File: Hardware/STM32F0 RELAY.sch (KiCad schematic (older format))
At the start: 22 parts, among them Q2 Q_NMOS_GSD, U10 STM32F030RCT6, Y3 32.768kHz, Y4 8MHz

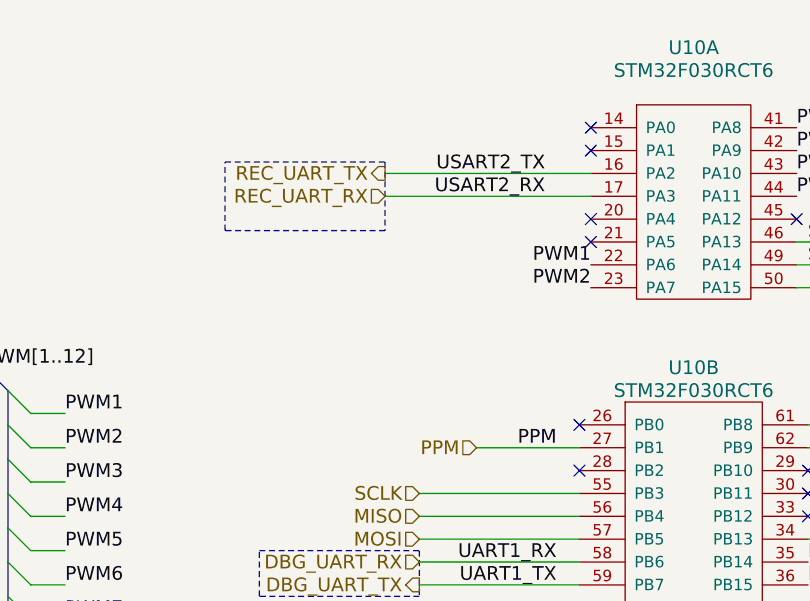
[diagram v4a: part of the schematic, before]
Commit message: Added RSSI, datasheets, INDU-004
Added RSSI input to PPM connector. Added datasheets for most of the components. The filter inductors for the FTDI were labeled as INDU-002, which is a 15uH smps inductor.
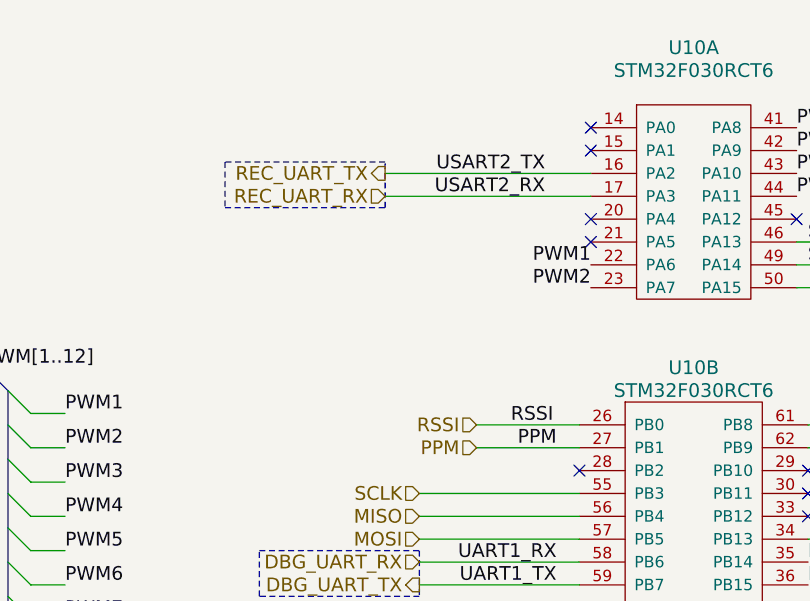
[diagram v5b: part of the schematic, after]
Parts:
- C46, C47, C48, C49, C50, C51, C52, C53, C54: footprint Resistors_SMD:R_0603_HandSoldering -> Capacitors_SMD:C_0603_HandSoldering
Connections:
- net RSSI: now reaches U10.26 (PB0)
- no-connect marks 18 -> 17
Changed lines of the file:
@@
 F 0 "C51" H 7225 5150 50  0000 L CNN
 F 1 "100nF" H 7225 4950 50  0000 L CNN
-F 2 "Resistors_SMD:R_0603_HandSoldering" H 7238 4900 50  0001 C CNN
-F 3 "" H 7200 5050 50  0001 C CNN
+F 2 "Capacitors_SMD:C_0603_HandSoldering" H 7238 4900 50  0001 C CNN
+F 3 "https://search.murata.co.jp/Ceramy/image/img/A01X/G101/ENG/GRM188R71E104KA01-01.pdf" H 7200 5050 50  0001 C CNN
 F 4 "CAPP-005" H 7200 5050 60  0001 C CNN "part_num"
 	1    7200 5050
@@
 F 0 "C52" H 7475 5150 50  0000 L CNN
 F 1 "4.7uF" H 7475 4950 50  0000 L CNN
-F 2 "Resistors_SMD:R_0603_HandSoldering" H 7488 4900 50  0001 C CNN
-F 3 "" H 7450 5050 50  0001 C CNN
+F 2 "Capacitors_SMD:C_0603_HandSoldering" H 7488 4900 50  0001 C CNN
+F 3 "http://www.samsungsem.com/kr/support/product-search/mlcc/CL10A475MP5LNNC.jsp" H 7450 5050 50  0001 C CNN
 F 4 "CAPP-006" H 7450 5050 60  0001 C CNN "part_num"
 	1    7450 5050
@@
 F 0 "C53" H 7725 5150 50  0000 L CNN
 F 1 "10nF" H 7725 4950 50  0000 L CNN
-F 2 "Resistors_SMD:R_0603_HandSoldering" H 7738 4900 50  0001 C CNN
-F 3 "" H 7700 5050 50  0001 C CNN
+F 2 "Capacitors_SMD:C_0603_HandSoldering" H 7738 4900 50  0001 C CNN
+F 3 "https://search.murata.co.jp/Ceramy/image/img/A01X/G101/ENG/GRM188R71H103KA01-01.pdf" H 7700 5050 50  0001 C CNN
 F 4 "CAPP-010" H 7700 5050 60  0001 C CNN "part_num"
 	1    7700 5050
@@
 F 0 "C50" H 6975 5150 50  0000 L CNN
 F 1 "100nF" H 6975 4950 50  0000 L CNN
-F 2 "Resistors_SMD:R_0603_HandSoldering" H 6988 4900 50  0001 C CNN
-F 3 "" H 6950 5050 50  0001 C CNN
+F 2 "Capacitors_SMD:C_0603_HandSoldering" H 6988 4900 50  0001 C CNN
+F 3 "https://search.murata.co.jp/Ceramy/image/img/A01X/G101/ENG/GRM188R71E104KA01-01.pdf" H 6950 5050 50  0001 C CNN
 F 4 "CAPP-005" H 6950 5050 60  0001 C CNN "part_num"
 	1    6950 5050
@@
 F 0 "C54" H 7975 5150 50  0000 L CNN
 F 1 "1uF" H 7975 4950 50  0000 L CNN
-F 2 "Resistors_SMD:R_0603_HandSoldering" H 7988 4900 50  0001 C CNN
-F 3 "" H 7950 5050 50  0001 C CNN
+F 2 "Capacitors_SMD:C_0603_HandSoldering" H 7988 4900 50  0001 C CNN
+F 3 "https://search.murata.co.jp/Ceramy/image/img/A01X/G101/ENG/GRM188R61E105KA12-01.pdf" H 7950 5050 50  0001 C CNN
 F 4 "CAPP-004" H 7950 5050 60  0001 C CNN "part_num"
 	1    7950 5050
@@
 F 1 "32.768kHz" H 7000 2150 50  0000 C CNN
 F 2 "Crystals:Crystal_SMD_MicroCrystal_CC7V-T1A-2pin_3.2x1.5mm_HandSoldering" H 7000 2300 50  0001 C CNN
-F 3 "" H 7000 2300 50  0001 C CNN
+F 3 "http://www.ecsxtal.com/store/pdf/ecx-31b.pdf" H 7000 2300 50  0001 C CNN
 F 4 "XTAL-001" H 7000 2300 60  0001 C CNN "part_num"
 	1    7000 2300
@@
 F 1 "8MHz" H 7000 2700 50  0000 C CNN
 F 2 "Crystals:Crystal_SMD_5032-2pin_5.0x3.2mm_HandSoldering" H 7000 2850 50  0001 C CNN
-F 3 "" H 7000 2850 50  0001 C CNN
+F 3 "https://abracon.com/Resonators/abm3.pdf" H 7000 2850 50  0001 C CNN
 F 4 "XTAL-002" H 7000 2850 60  0001 C CNN "part_num"
 	1    7000 2850
@@
 F 0 "C48" H 6575 2800 50  0000 L CNN
 F 1 "7pF" H 6575 2600 50  0000 L CNN
-F 2 "Resistors_SMD:R_0603_HandSoldering" H 6588 2550 50  0001 C CNN
-F 3 "" H 6550 2700 50  0001 C CNN
+F 2 "Capacitors_SMD:C_0603_HandSoldering" H 6588 2550 50  0001 C CNN
+F 3 "https://katalog.we-online.de/pbs/datasheet/885012006031.pdf" H 6550 2700 50  0001 C CNN
 F 4 "CAPP-009" H 6550 2700 60  0001 C CNN "part_num"
 	1    6550 2700
@@
 F 0 "C49" H 6575 3100 50  0000 L CNN
 F 1 "7pF" H 6575 2900 50  0000 L CNN
-F 2 "Resistors_SMD:R_0603_HandSoldering" H 6588 2850 50  0001 C CNN
-F 3 "" H 6550 3000 50  0001 C CNN
+F 2 "Capacitors_SMD:C_0603_HandSoldering" H 6588 2850 50  0001 C CNN
+F 3 "https://katalog.we-online.de/pbs/datasheet/885012006031.pdf" H 6550 3000 50  0001 C CNN
 F 4 "CAPP-009" H 6550 3000 60  0001 C CNN "part_num"
 	1    6550 3000
@@
 F 0 "C47" H 6575 2550 50  0000 L CNN
 F 1 "14pF" H 6575 2350 50  0000 L CNN
-F 2 "Resistors_SMD:R_0603_HandSoldering" H 6588 2300 50  0001 C CNN
-F 3 "" H 6550 2450 50  0001 C CNN
+F 2 "Capacitors_SMD:C_0603_HandSoldering" H 6588 2300 50  0001 C CNN
+F 3 "https://katalog.we-online.de/pbs/datasheet/885012006033.pdf" H 6550 2450 50  0001 C CNN
 F 4 "CAPP-008" H 6550 2450 60  0001 C CNN "part_num"
 	1    6550 2450
@@
 F 0 "C46" H 6575 2250 50  0000 L CNN
 F 1 "14pF" H 6575 2050 50  0000 L CNN
-F 2 "Resistors_SMD:R_0603_HandSoldering" H 6588 2000 50  0001 C CNN
-F 3 "" H 6550 2150 50  0001 C CNN
+F 2 "Capacitors_SMD:C_0603_HandSoldering" H 6588 2000 50  0001 C CNN
+F 3 "https://katalog.we-online.de/pbs/datasheet/885012006033.pdf" H 6550 2150 50  0001 C CNN
 F 4 "CAPP-008" H 6550 2150 60  0001 C CNN "part_num"
 	1    6550 2150
@@
 Wire Notes Line
 	2500 4400 3200 4400
-Wire Notes Line
-	3050 2700 3050 3000
-Wire Notes Line
-	3050 3000 2350 3000
-Wire Notes Line
-	2350 3000 2350 2700
-Wire Notes Line
-	2350 2700 3050 2700
 $Comp
 L Device:LED D8
@@
 F 1 "LED" H 5800 5650 50  0000 C CNN
 F 2 "LEDs:LED_0603" H 5800 5750 50  0001 C CNN
-F 3 "" H 5800 5750 50  0001 C CNN
+F 3 "http://optoelectronics.liteon.com/upload/download/DS22-2000-228/LTST-C191KGKT.PDF" H 5800 5750 50  0001 C CNN
 F 4 "DIOD-002" H 5800 5750 60  0001 C CNN "part_num"
 	1    5800 5750
@@
 F 1 "LED" H 5450 5650 50  0000 C CNN
 F 2 "LEDs:LED_0603" H 5450 5750 50  0001 C CNN
-F 3 "" H 5450 5750 50  0001 C CNN
+F 3 "http://optoelectronics.liteon.com/upload/download/DS22-2000-228/LTST-C191KGKT.PDF" H 5450 5750 50  0001 C CNN
 F 4 "DIOD-002" H 5450 5750 60  0001 C CNN "part_num"
 	1    5450 5750
@@
 F 1 "LED" H 6150 5650 50  0000 C CNN
 F 2 "LEDs:LED_0603" H 6150 5750 50  0001 C CNN
-F 3 "" H 6150 5750 50  0001 C CNN
+F 3 "http://optoelectronics.liteon.com/upload/download/DS22-2000-228/LTST-C191KGKT.PDF" H 6150 5750 50  0001 C CNN
 F 4 "DIOD-002" H 6150 5750 60  0001 C CNN "part_num"
 	1    6150 5750
@@
 F 1 "Buzzer" H 6750 3900 50  0000 L CNN
 F 2 "WARG:AI-1027-TWT-3V-R" V 6575 4050 50  0001 C CNN
-F 3 "" V 6575 4050 50  0001 C CNN
+F 3 "http://www.puiaudio.com/pdf/AI-1027-TWT-5V-R.pdf" V 6575 4050 50  0001 C CNN
 F 4 "BUZZ-001" H 6600 3950 60  0001 C CNN "part_num"
 	1    6600 3950
@@
 Connection ~ 8900 4350
 NoConn ~ 3900 4050
-NoConn ~ 3900 3850
 NoConn ~ 4900 4050
 NoConn ~ 4900 4150
@@
 Wire Wire Line
 	5800 4500 5800 4600
+Text HLabel 3450 3850 0    60   Input ~ 0
+RSSI
+Wire Wire Line
+	3450 3850 3900 3850
+Text Label 3600 3850 0    60   ~ 0
+RSSI
+Wire Notes Line
+	3050 2700 2350 2700
+Wire Notes Line
+	2350 2700 2350 2900
+Wire Notes Line
+	2350 2900 3050 2900
+Wire Notes Line
+	3050 2900 3050 2700
 Wire Bus Line
 	1400 3700 1400 5350
